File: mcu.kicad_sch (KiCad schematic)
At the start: 17 parts, among them J12 MCU_GPIOS, U1 TLV709A33DBVR, U2 ATmega168A-A, Y1 16M

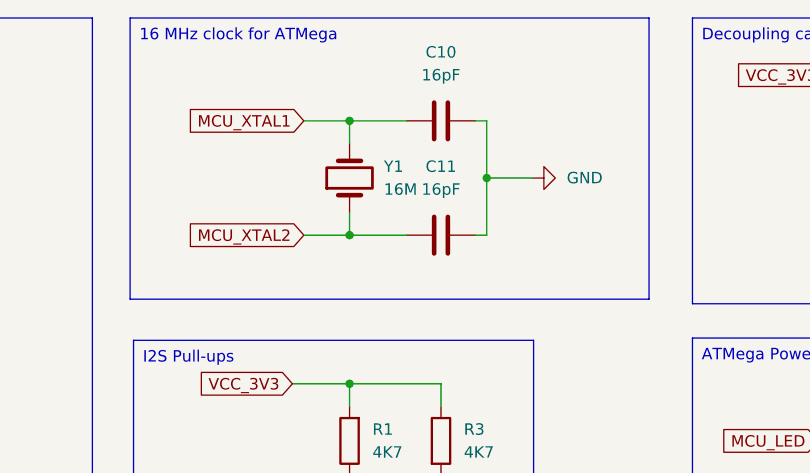
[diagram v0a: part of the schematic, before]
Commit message: 16M mcu crystal changed to 12M
- Atmel168A crystal max frequency can be about
  13.3 Mhz for 3V3 voltage.
  See atmega168a datasheet Figure 29-1. Maximum Frequency vs. VCC
--> 10MHz + 10Mhz/(4.5 - 2.7) * (3.3 - 2.7) = 13.3Mhz

Signed-off-by: Mika Laitio <lamikr@gmail.com>
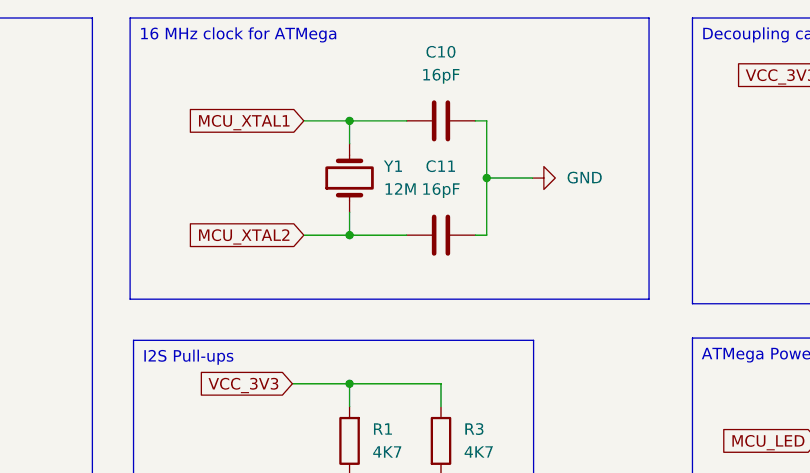
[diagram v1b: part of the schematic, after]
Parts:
- Y1: value 16M -> 12M; footprint lamikr_audio:XTAL_ABM7_ABR -> lamikr_audio:XTAL_ABM7-12.000MHZ-D2Y-T; MPN ABM7-16.000MHZ-D2Y-T -> ABM7-12.000MHZ-D2Y-T; SKU_DIGIKEY 535-9840-1-ND -> 535-9836-1-ND
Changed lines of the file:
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@@
+	)
+	(symbol
+		(lib_id "Device:Crystal")
+		(at 134.62 36.83 90)
+		(unit 1)
+		(exclude_from_sim no)
+		(in_bom yes)
+		(on_board yes)
+		(dnp no)
+		(fields_autoplaced yes)
+		(property "Reference" "Y1"
+			(at 138.43 35.56 90)
+			(effects
+				(font
+					(size 1.27 1.27)
+				)
+				(justify right)
+			)
+		)
+		(property "Value" "12M"
+			(at 138.43 38.1 90)
+			(effects
+				(font
+					(size 1.27 1.27)
+				)
+				(justify right)
+			)
+		)
+		(property "Footprint" "lamikr_audio:XTAL_ABM7-12.000MHZ-D2Y-T"
+			(at 134.62 36.83 0)
+			(effects
+				(font
+					(size 1.27 1.27)
+				)
+				(hide yes)
+			)
+		)
+		(property "Datasheet" "~"
+			(at 134.62 36.83 0)
+			(effects
+				(font
+					(size 1.27 1.27)
+				)
+				(hide yes)
+			)
+		)
+		(property "Description" "Two pin crystal"
+			(at 134.62 36.83 0)
+			(effects
+				(font
+					(size 1.27 1.27)
+				)
+				(hide yes)
+			)
+		)
+		(property "SKU_DIGIKEY" "535-9836-1-ND"
+			(at 134.62 36.83 90)
+			(effects
+				(font
+					(size 1.27 1.27)
+				)
+				(hide yes)
+			)
+		)
+		(property "Notes" ""
+			(at 134.62 36.83 0)
+			(effects
+				(font
+					(size 1.27 1.27)
+				)
+				(hide yes)
+			)
+		)
+		(property "Price" "0.67"
+			(at 134.62 36.83 0)
+			(effects
+				(font
+					(size 1.27 1.27)
+				)
+				(hide yes)
+			)
+		)
+		(property "MFR" "Abracon LLC"
+			(at 134.62 36.83 0)
+			(effects
+				(font
+					(size 1.27 1.27)
+				)
+				(hide yes)
+			)
+		)
+		(property "MPN" "ABM7-12.000MHZ-D2Y-T"
+			(at 134.62 36.83 0)
+			(effects
+				(font
+					(size 1.27 1.27)
+				)
+				(hide yes)
+			)
+		)
+		(property "QtyOrdered" "10"
+			(at 134.62 36.83 0)
+			(effects
+				(font
+					(size 1.27 1.27)
+				)
+				(hide yes)
+			)
+		)
+		(pin "1"
+		)
+		(pin "2"
+		)
+		(instances
+			(project "i2s_to_toslink_pcb"
+				(path "/d64b6b4a-9bae-4214-91d3-9beeedeca582/b556b917-e298-4f65-bb14-1be62415fc17"
+					(reference "Y1")
+					(unit 1)
+				)
+			)
+		)
 	)
 	(symbol
@@
 					(unit 1)
 				)
-			)
-		)
-	)
-	(symbol
-		(lib_id "Device:Crystal")
-		(at 134.62 36.83 90)
-		(unit 1)
-		(exclude_from_sim no)
-		(in_bom yes)
-		(on_board yes)
-		(dnp no)
-		(fields_autoplaced yes)
-		(property "Reference" "Y1"
-			(at 138.43 35.56 90)
-			(effects
-				(font
-					(size 1.27 1.27)
-				)
-				(justify right)
-			)
-		)
-		(property "Value" "16M"
-			(at 138.43 38.1 90)
-			(effects
-				(font
-					(size 1.27 1.27)
-				)
-				(justify right)
-			)
-		)
-		(property "Footprint" "lamikr_audio:XTAL_ABM7_ABR"
-			(at 134.62 36.83 0)
-			(effects
-				(font
-					(size 1.27 1.27)
-				)
-				(hide yes)
-			)
-		)
-		(property "Datasheet" "~"
-			(at 134.62 36.83 0)
-			(effects
-				(font
-					(size 1.27 1.27)
-				)
-				(hide yes)
-			)
-		)
-		(property "Description" "Two pin crystal"
-			(at 134.62 36.83 0)
-			(effects
-				(font
-					(size 1.27 1.27)
-				)
-				(hide yes)
-			)
-		)
-		(property "SKU_DIGIKEY" "535-9840-1-ND"
-			(at 134.62 36.83 90)
-			(effects
-				(font
-					(size 1.27 1.27)
-				)
-				(hide yes)
-			)
-		)
-		(property "Notes" ""
-			(at 134.62 36.83 0)
-			(effects
-				(font
-					(size 1.27 1.27)
-				)
-				(hide yes)
-			)
-		)
-		(property "Price" "0.67"
-			(at 134.62 36.83 0)
-			(effects
-				(font
-					(size 1.27 1.27)
-				)
-				(hide yes)
-			)
-		)
-		(property "MFR" "Abracon LLC"
-			(at 134.62 36.83 0)
-			(effects
-				(font
-					(size 1.27 1.27)
-				)
-				(hide yes)
-			)
-		)
-		(property "MPN" "ABM7-16.000MHZ-D2Y-T"
-			(at 134.62 36.83 0)
-			(effects
-				(font
-					(size 1.27 1.27)
-				)
-				(hide yes)
-			)
-		)
-		(property "QtyOrdered" "10"
-			(at 134.62 36.83 0)
-			(effects
-				(font
-					(size 1.27 1.27)
-				)
-				(hide yes)
-			)
-		)
-		(pin "1"
-		)
-		(pin "2"
-		)
-		(instances
-			(project "i2s_to_toslink_pcb"
-				(path "/d64b6b4a-9bae-4214-91d3-9beeedeca582/b556b917-e298-4f65-bb14-1be62415fc17"
-					(reference "Y1")
-					(unit 1)
-				)

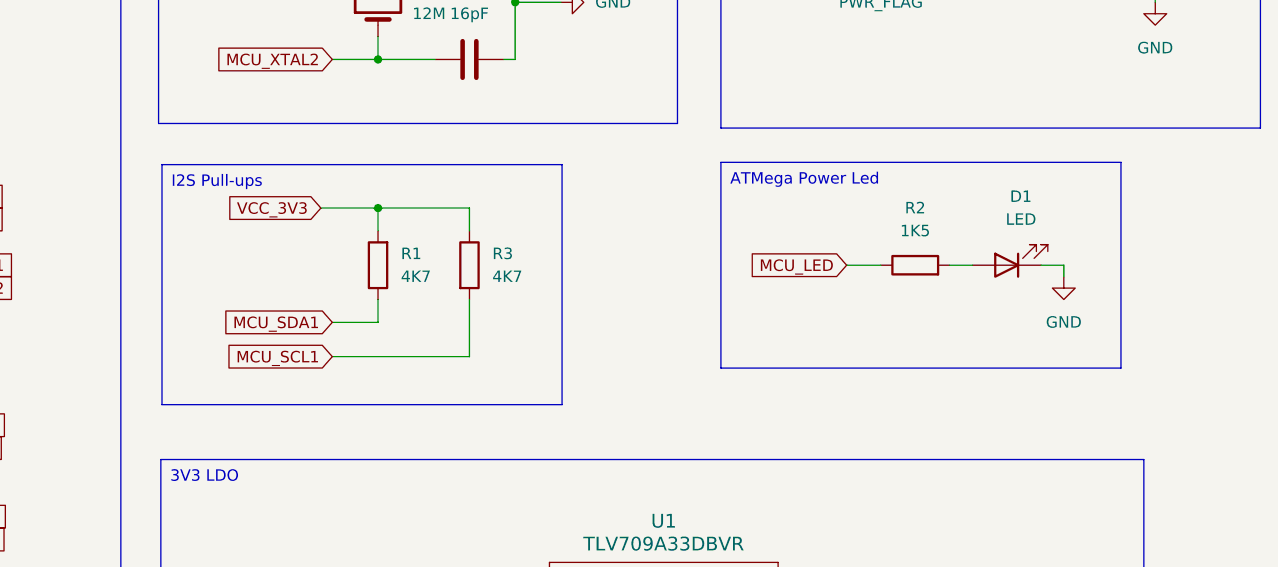
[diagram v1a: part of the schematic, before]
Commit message: add pull-up resistors for codex rx-pins
- add connectors for rx0 and rx1 pins
- rest of the rx-pins not reserved for use
  and they will share a common pull-up.

Signed-off-by: Mika Laitio <lamikr@gmail.com>
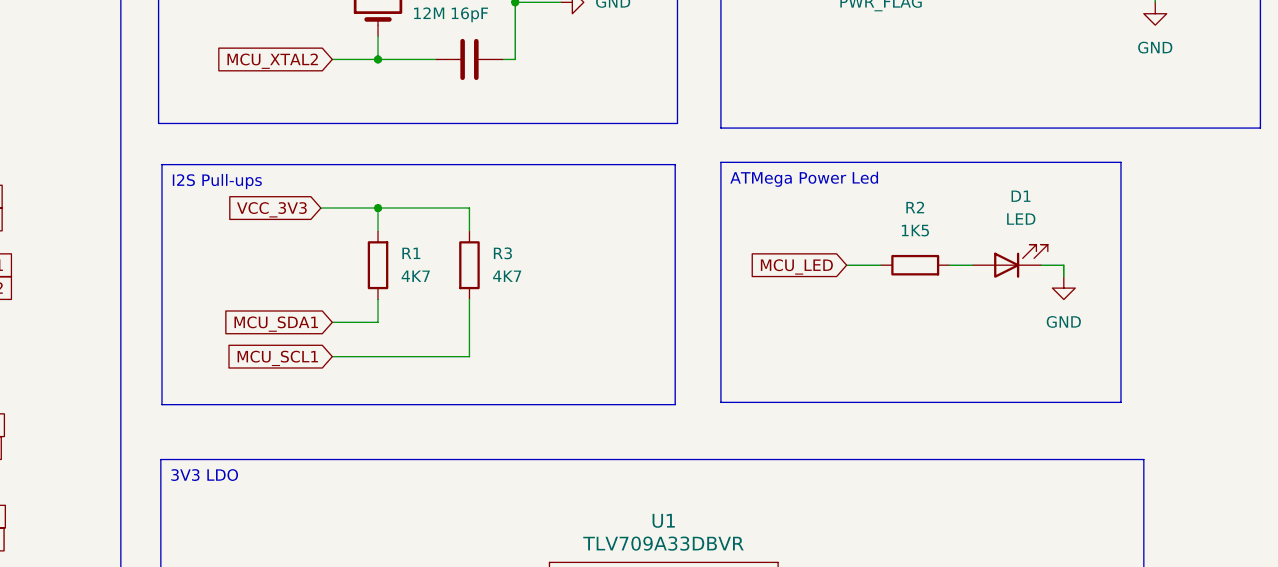
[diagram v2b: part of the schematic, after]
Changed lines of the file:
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@@
 		(exclude_from_sim no)
 		(at 172.72 54.61 0)
-		(size 44.45 22.86)
+		(size 44.45 26.67)
 		(stroke
 			(width 0)
@@
 		(exclude_from_sim no)
 		(at 110.617 54.864 0)
-		(size 44.45 26.67)
+		(size 57.023 26.67)
 		(stroke
 			(width 0)

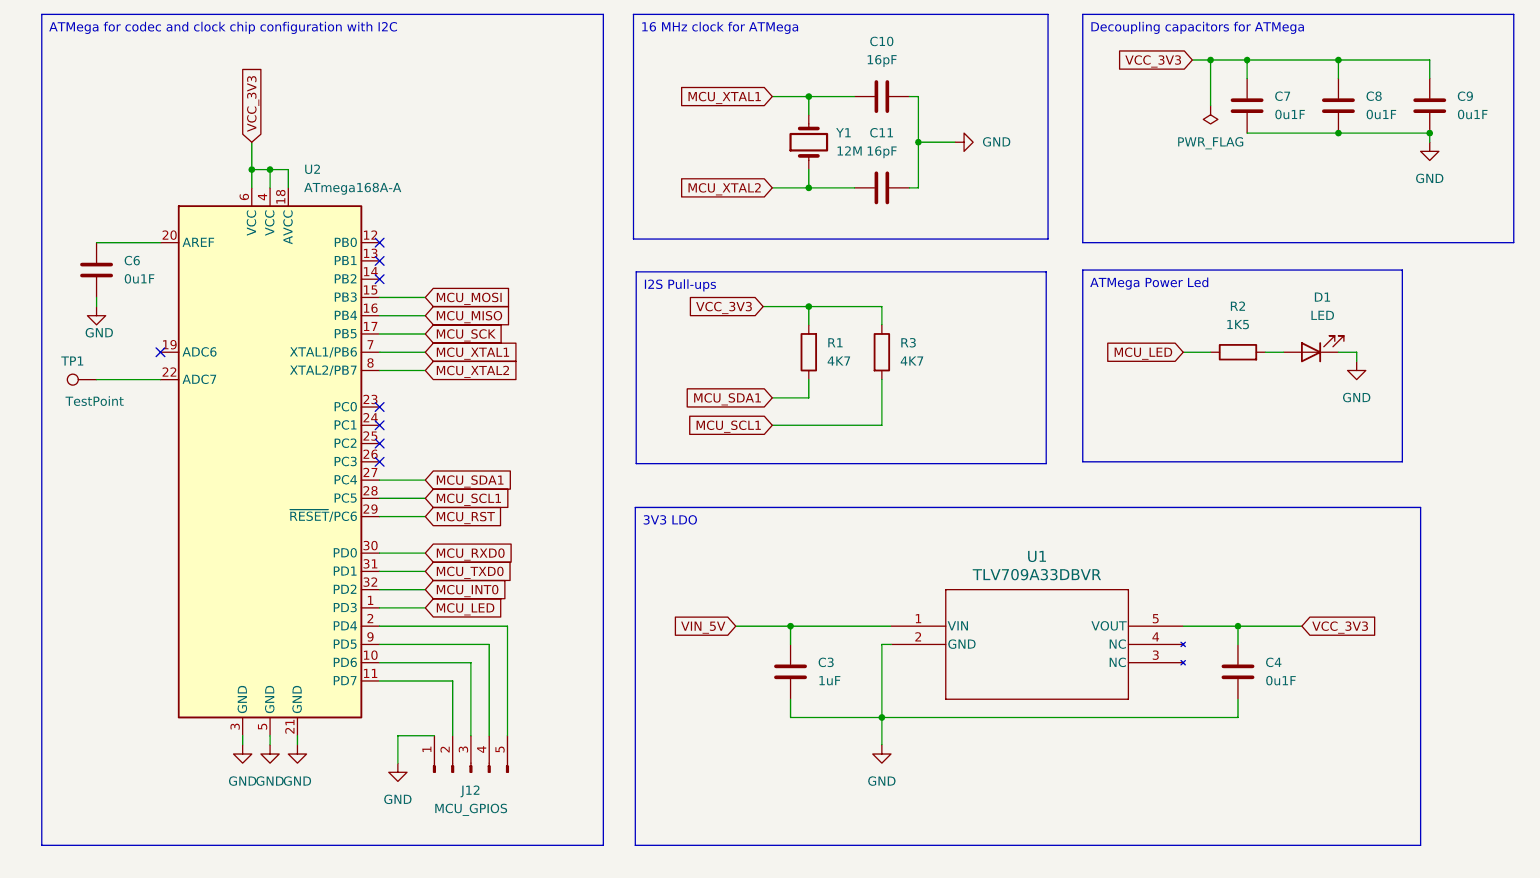
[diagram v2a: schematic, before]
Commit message: rework the atmega168 reset signal schematics and routing
Signed-off-by: Mika Laitio <lamikr@gmail.com>
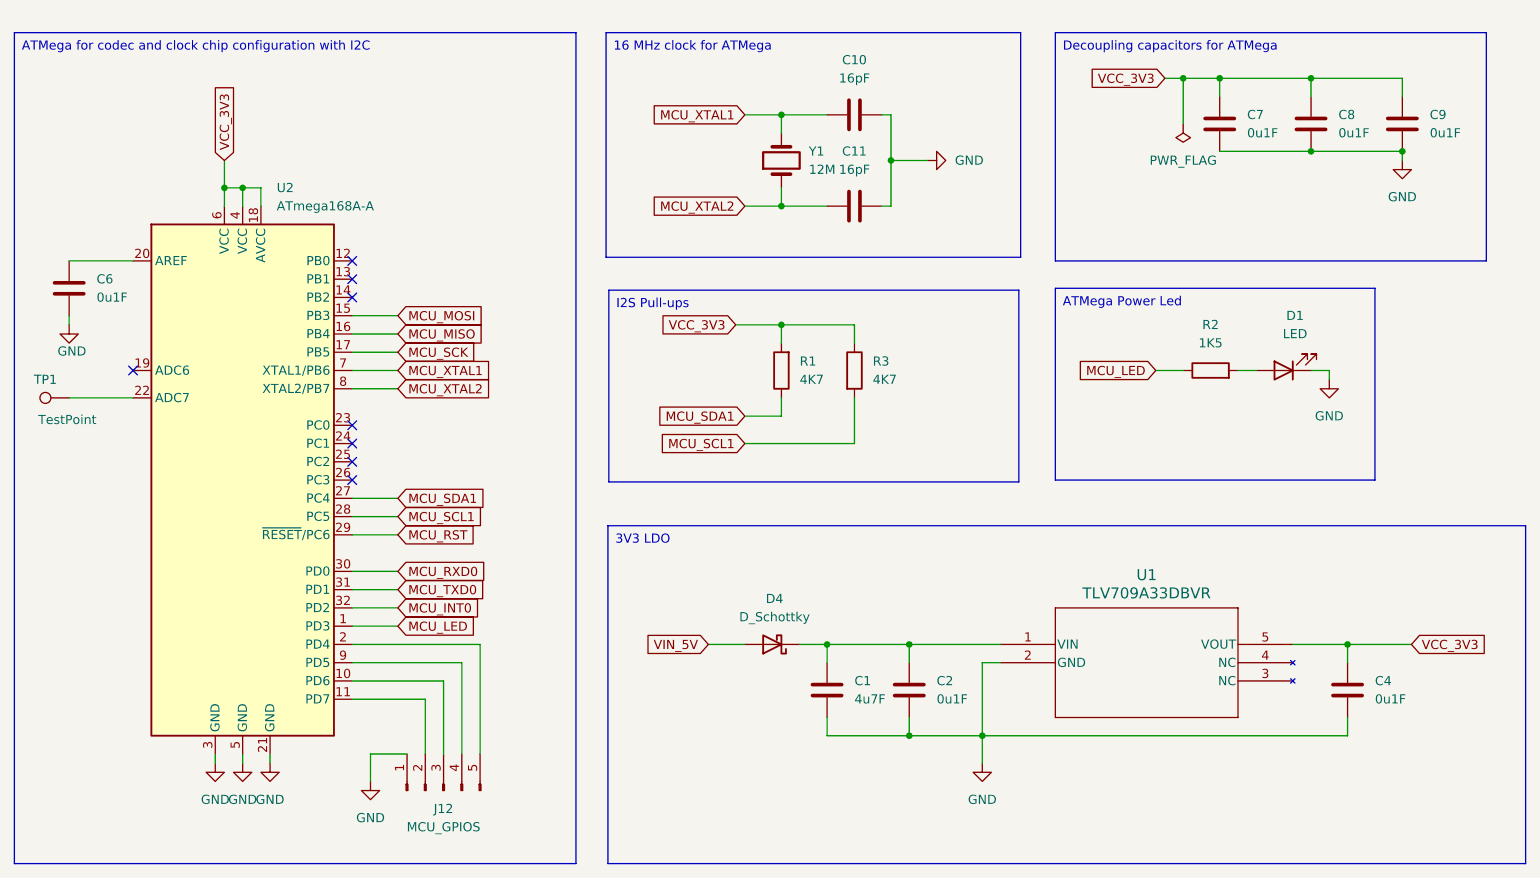
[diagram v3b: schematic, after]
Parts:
- removed C3: 1uF, Capacitor_SMD:C_0603_1608Metric, symbol Device:C
- added C1: 4u7F, Capacitor_SMD:C_0603_1608Metric, symbol Device:C
- added C2: 0u1F, Capacitor_SMD:C_0603_1608Metric, symbol Device:C
- added D4: D_Schottky, Diode_SMD:D_0603_1608Metric, symbol Device:D_Schottky
- C7, C8: footprint Capacitor_SMD:C_0402_1005Metric -> Capacitor_SMD:C_0603_1608Metric
- R1, R3: footprint Resistor_SMD:R_0402_1005Metric -> Resistor_SMD:R_0603_1608Metric
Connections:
- net GND: now also C1.2, C2.2
- net VIN_5V: now also D4.2 (A); no longer U1.1 (VIN)
- new net: C1.1, C2.1, D4.1 (K), U1.1 (VIN)
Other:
- moved on the sheet: C10, C11, C4, C6, C7, C8, C9, D1, J12, R1, R2, R3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
